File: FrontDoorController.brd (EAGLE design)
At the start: 31.4 x 49.1 mm, 9 parts

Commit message: Door_Control_PCB: Add more header pins
Add more header pins to be able to measure all voltages, and connect to
the limit switches on the Lockitron to log the deadbolt position.  Also
reroute the motor drive wires to not go through the Photon through hole
pins and make the wires larger to drive more current.
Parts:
- JP1: device SparkFun-Connectors:1X05 -> SparkFun-Connectors:1X10_LOCK
- moved JP1 6.69 mm to (3.97, 3.34)
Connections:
- removed net D0: U$1.13, U$3.13
- removed net D1: U$1.14, U$3.14
- new net N$7: JP1.10
- new net SW1: JP1.8, U$1.13, U$3.13
- new net SW2: JP1.9, U$1.14, U$3.14
- net 3V3: now also JP1.6
- net VIN: now also JP1.5
- net VM: now also JP1.7; no longer JP1.5
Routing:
- net 3V3: track 1.27 -> 60.3 mm
- net SW2: track 0.00 -> 18.1 mm
- net SW1: track 0.00 -> 17.3 mm
- net VIN: track 67.9 -> 72.9 mm
- net A02: track 40.2 -> 35.9 mm
- net A01: track 35.9 -> 31.7 mm
- net D1: track 1.27 -> 0.00 mm
- net D0: track 1.27 -> 0.00 mm
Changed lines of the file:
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@@
 <attribute name="NAME" x="16.291" y="40.1415" size="0.4064" layer="26" rot="MR180"/>
 </element>
-<element name="JP1" library="SparkFun-Connectors" package="1X05" value="" x="10.66" y="3.32" smashed="yes">
-<attribute name="VALUE" x="9.39" y="0.145" size="1.27" layer="27"/>
+<element name="JP1" library="SparkFun-Connectors" package="1X10_LOCK" value="" x="3.97" y="3.34" smashed="yes">
+<attribute name="VALUE" x="2.7" y="0.165" size="1.27" layer="27"/>
 </element>
 <element name="D1" library="SparkFun-DiscreteSemi" package="DIODE-1N4001" value="" x="15.67" y="7.01" smashed="yes" rot="R180">
@@
 <wire x1="10.59" y1="7.01" x2="5.99" y2="7.01" width="1.016" layer="1"/>
 <wire x1="5.99" y1="7.01" x2="2" y2="11" width="1.016" layer="1"/>
+<contactref element="JP1" pad="5"/>
+<wire x1="10.59" y1="7.01" x2="10.59" y2="7.007" width="1.016" layer="1"/>
+<wire x1="10.59" y1="7.007" x2="14.13" y2="3.467" width="1.016" layer="1"/>
 </signal>
 <signal name="GND">
@@
 <contactref element="JP1" pad="4"/>
 <contactref element="JP1" pad="3"/>
-<polygon width="0.4064" layer="16">
+<polygon width="0.4064" layer="16" thermals="no">
 <vertex x="1" y="48"/>
 <vertex x="28" y="48"/>
@@
 <wire x1="25.89" y1="44.418" x2="24.63" y2="44.418" width="1.016" layer="1"/>
 <wire x1="24.63" y1="44.418" x2="24.62" y2="44.428" width="1.016" layer="1"/>
+<contactref element="JP1" pad="6"/>
+<wire x1="16.67" y1="3.213" x2="16.67" y2="2.11" width="0.4064" layer="16"/>
+<wire x1="29.02" y1="2.96" x2="29.02" y2="42.88" width="0.4064" layer="16"/>
+<wire x1="29.02" y1="42.88" x2="27.55" y2="44.35" width="0.4064" layer="16"/>
+<wire x1="27.55" y1="44.35" x2="24.698" y2="44.35" width="0.4064" layer="16"/>
+<wire x1="24.698" y1="44.35" x2="24.62" y2="44.428" width="0.4064" layer="16"/>
+<wire x1="16.67" y1="2.11" x2="17.04" y2="1.74" width="0.4064" layer="16"/>
+<wire x1="17.04" y1="1.74" x2="27.8" y2="1.74" width="0.4064" layer="16"/>
+<wire x1="27.8" y1="1.74" x2="29.02" y2="2.96" width="0.4064" layer="16"/>
 </signal>
 <signal name="RSTB">
@@
 <wire x1="25.88" y1="21.568" x2="25.89" y2="21.558" width="1.016" layer="1"/>
 </signal>
-<signal name="D1">
-<contactref element="U$1" pad="14"/>
-<contactref element="U$3" pad="14"/>
-<wire x1="24.62" y1="19.028" x2="25.88" y2="19.028" width="1.016" layer="1"/>
-<wire x1="25.88" y1="19.028" x2="25.89" y2="19.018" width="1.016" layer="1"/>
-</signal>
-<signal name="D0">
-<contactref element="U$1" pad="13"/>
-<contactref element="U$3" pad="13"/>
-<wire x1="24.62" y1="16.488" x2="25.88" y2="16.488" width="1.016" layer="1"/>
-<wire x1="25.88" y1="16.488" x2="25.89" y2="16.478" width="1.016" layer="1"/>
-</signal>
 <signal name="USB_D+">
 <contactref element="U$1" pad="31"/>
@@
 <contactref element="U$2" pad="2"/>
 <contactref element="JP1" pad="2"/>
-<wire x1="12.584" y1="30.155" x2="12.584" y2="30.805" width="0.4064" layer="16"/>
-<wire x1="12.584" y1="30.155" x2="12.584" y2="25.144" width="0.4064" layer="16"/>
-<wire x1="12.584" y1="25.144" x2="5.92" y2="18.48" width="0.4064" layer="16"/>
-<wire x1="5.92" y1="7.22" x2="5.92" y2="18.48" width="0.4064" layer="16"/>
-<wire x1="5.92" y1="7.22" x2="8" y2="5.14" width="0.4064" layer="16"/>
-<wire x1="8" y1="5.14" x2="12.47" y2="5.14" width="0.4064" layer="16"/>
-<wire x1="12.47" y1="5.14" x2="13.2" y2="4.41" width="0.4064" layer="16"/>
-<wire x1="13.2" y1="4.41" x2="13.2" y2="3.32" width="0.4064" layer="16"/>
+<wire x1="12.584" y1="30.805" x2="11.885" y2="30.805" width="0.4064" layer="16"/>
+<wire x1="11.885" y1="30.805" x2="11.52" y2="30.44" width="0.4064" layer="16"/>
+<wire x1="11.52" y1="30.44" x2="11.805" y2="30.155" width="0.4064" layer="16"/>
+<wire x1="11.805" y1="30.155" x2="12.584" y2="30.155" width="0.4064" layer="16"/>
+<wire x1="6.51" y1="3.213" x2="6.51" y2="10.51" width="1.016" layer="16"/>
+<wire x1="6.51" y1="10.51" x2="11" y2="15" width="1.016" layer="16"/>
+<wire x1="11" y1="15" x2="11" y2="29.92" width="1.016" layer="16"/>
+<wire x1="11" y1="29.92" x2="11.52" y2="30.44" width="1.016" layer="16"/>
 </signal>
 <signal name="A02">
@@
 <contactref element="U$2" pad="6"/>
 <contactref element="JP1" pad="1"/>
-<wire x1="12.584" y1="33.405" x2="12.584" y2="32.755" width="0.4064" layer="16"/>
-<wire x1="12.584" y1="32.755" x2="11.095" y2="32.755" width="0.4064" layer="16"/>
-<wire x1="11.095" y1="32.755" x2="10.45" y2="32.11" width="0.4064" layer="16"/>
-<wire x1="10.45" y1="32.11" x2="10.45" y2="25.58" width="0.4064" layer="16"/>
-<wire x1="10.45" y1="25.58" x2="3.94" y2="19.07" width="0.4064" layer="16"/>
-<wire x1="3.94" y1="19.07" x2="3.94" y2="5.06" width="0.4064" layer="16"/>
-<wire x1="3.94" y1="5.06" x2="5.68" y2="3.32" width="0.4064" layer="16"/>
-<wire x1="5.68" y1="3.32" x2="10.66" y2="3.32" width="0.4064" layer="16"/>
+<wire x1="12.584" y1="32.755" x2="11.915" y2="32.755" width="0.4064" layer="16"/>
+<wire x1="11.915" y1="32.755" x2="11.59" y2="33.08" width="0.4064" layer="16"/>
+<wire x1="11.59" y1="33.08" x2="11.915" y2="33.405" width="0.4064" layer="16"/>
+<wire x1="11.915" y1="33.405" x2="12.584" y2="33.405" width="0.4064" layer="16"/>
+<wire x1="3.97" y1="3.467" x2="3.97" y2="9.97" width="1.016" layer="16"/>
+<wire x1="3.97" y1="9.97" x2="9" y2="15" width="1.016" layer="16"/>
+<wire x1="9" y1="15" x2="9" y2="32" width="1.016" layer="16"/>
+<wire x1="9" y1="32" x2="10.08" y2="33.08" width="1.016" layer="16"/>
+<wire x1="10.08" y1="33.08" x2="11.59" y2="33.08" width="1.016" layer="16"/>
 </signal>
 <signal name="VM">
@@
 <contactref element="U$2" pad="24"/>
 <contactref element="C1" pad="A"/>
-<contactref element="JP1" pad="5"/>
 <contactref element="C2" pad="1"/>
 <wire x1="18.14" y1="24.76" x2="18.07" y2="24.76" width="0.4064" layer="16"/>
@@
 <wire x1="18.1" y1="36.685" x2="18.1" y2="36.76" width="0.4064" layer="16"/>
 <contactref element="D1" pad="A"/>
-<polygon width="0.4064" layer="1">
+<polygon width="0.4064" layer="1" thermals="no">
 <vertex x="1" y="48"/>
 <vertex x="28" y="48"/>
@@
 <wire x1="18.345" y1="36.655" x2="18.205" y2="36.655" width="0.6096" layer="16"/>
 <wire x1="18.205" y1="36.655" x2="18.1" y2="36.76" width="0.6096" layer="16" curve="-90"/>
+<contactref element="JP1" pad="7"/>
 </signal>
 <signal name="N$3">
@@
 <wire x1="24.63" y1="39.338" x2="24.62" y2="39.348" width="1.016" layer="1"/>
 </signal>
+<signal name="SW1">
+<contactref element="JP1" pad="8"/>
+<contactref element="U$1" pad="13"/>
+<wire x1="21.75" y1="3.213" x2="21.75" y2="4.75" width="0.4064" layer="16"/>
+<wire x1="21.75" y1="4.75" x2="25" y2="8" width="0.4064" layer="16"/>
+<contactref element="U$3" pad="13"/>
+<wire x1="24.62" y1="16.488" x2="25.88" y2="16.488" width="1.016" layer="1"/>
+<wire x1="25.89" y1="16.478" x2="24.63" y2="16.478" width="0.4064" layer="1"/>
+<wire x1="24.63" y1="16.478" x2="24.62" y2="16.488" width="0.4064" layer="1"/>
+<wire x1="25" y1="8" x2="25" y2="16.108" width="0.4064" layer="16"/>
+<wire x1="25" y1="16.108" x2="24.62" y2="16.488" width="0.4064" layer="16"/>
+</signal>
+<signal name="SW2">
+<contactref element="JP1" pad="9"/>
+<contactref element="U$1" pad="14"/>
+<contactref element="U$3" pad="14"/>
+<wire x1="24.62" y1="19.028" x2="25.88" y2="19.028" width="1.016" layer="1"/>
+<wire x1="24.29" y1="3.467" x2="24.29" y2="6.29" width="0.4064" layer="16"/>
+<wire x1="24.29" y1="6.29" x2="26" y2="8" width="0.4064" layer="16"/>
+<wire x1="26" y1="8" x2="26" y2="17.648" width="0.4064" layer="16"/>
+<wire x1="26" y1="17.648" x2="24.62" y2="19.028" width="0.4064" layer="16"/>
+<wire x1="25.88" y1="19.028" x2="25.89" y2="19.018" width="0" layer="19" extent="1-1"/>
+</signal>
+<signal name="N$7">
+<contactref element="JP1" pad="10"/>
+</signal>
 </signals>

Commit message: Door_Control_PCB: Add reed switch connection
Add a connection point for a reed switch to be used to sense if the door
is open or closed.  Also add a pull down resistor to ensure good
readings and label the pins on the header.
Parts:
- added R1: 1K, SparkFun-Resistors:0603-RES
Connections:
- removed net D2: U$1.15, U$3.15
- removed net N$7: JP1.10
- new net DOORSW: JP1.10, R1.2, U$1.15, U$3.15
- net GND: now also R1.1
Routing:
- net DOORSW: track 0.00 -> 25.0 mm
- net D2: track 1.27 -> 0.00 mm
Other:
- board text added: "3V3"
- board text added: "A01"
- board text added: "A02"
- board text added: "DOORSW"
- board text added: "GND"
- board text added: "SW1"
- board text added: "SW2"
- board text added: "VIN"
- board text added: "VM"
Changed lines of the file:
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@@
 <dimension x1="0" y1="0" x2="0" y2="49" x3="-4" y3="24.5" textsize="1.778" layer="48" unit="inch"/>
 <dimension x1="0" y1="0" x2="31.42" y2="0" x3="15.71" y3="-4" textsize="1.778" layer="48" unit="inch"/>
+<text x="3.13" y="1" size="0.6096" layer="51">A02</text>
+<text x="5.7" y="1" size="0.6096" layer="51">A01</text>
+<text x="9.45" y="1" size="0.6096" layer="51">GND</text>
+<text x="13.35" y="1" size="0.6096" layer="51">VIN</text>
+<text x="16" y="1" size="0.6096" layer="51">3V3</text>
+<text x="18.59" y="1.01" size="0.6096" layer="51">VM</text>
+<text x="20.82" y="1" size="0.6096" layer="51">SW1</text>
+<text x="23.4" y="1" size="0.6096" layer="51">SW2</text>
+<text x="26" y="1" size="0.6096" layer="51">DOORSW</text>
 </plain>
 <attributes>
@@
 </element>
 <element name="U$3" library="Spark" package="PHOTON" value="PHOTON_WITH_HEADERS" x="5.57" y="12.17" smashed="yes"/>
+<element name="R1" library="SparkFun-Resistors" package="0603-RES" value="1K" x="21.5" y="21.69" rot="MR180"/>
 </elements>
 <signals>
@@
 <wire x1="25.89" y1="36.79" x2="24.638" y2="36.79" width="1.016" layer="1"/>
 <wire x1="24.638" y1="36.79" x2="24.62" y2="36.808" width="1.016" layer="1"/>
+<contactref element="R1" pad="1"/>
 </signal>
 <signal name="TX">
@@
 <wire x1="19.896" y1="33.405" x2="22.943" y2="33.405" width="0.4064" layer="16"/>
 <wire x1="22.943" y1="33.405" x2="24.62" y2="31.728" width="0.4064" layer="16"/>
-</signal>
-<signal name="D2">
-<contactref element="U$1" pad="15"/>
-<contactref element="U$3" pad="15"/>
-<wire x1="24.62" y1="21.568" x2="25.88" y2="21.568" width="1.016" layer="1"/>
-<wire x1="25.88" y1="21.568" x2="25.89" y2="21.558" width="1.016" layer="1"/>
 </signal>
 <signal name="USB_D+">
@@
 <wire x1="25.88" y1="19.028" x2="25.89" y2="19.018" width="0" layer="19" extent="1-1"/>
 </signal>
-<signal name="N$7">
+<signal name="DOORSW">
 <contactref element="JP1" pad="10"/>
+<contactref element="U$1" pad="15"/>
+<contactref element="U$3" pad="15"/>
+<wire x1="24.62" y1="21.568" x2="25.88" y2="21.568" width="1.016" layer="1"/>
+<wire x1="26.83" y1="3.213" x2="29" y2="5.383" width="0.4064" layer="1"/>
+<wire x1="27.442" y1="21.558" x2="25.89" y2="21.558" width="0.4064" layer="1"/>
+<wire x1="29" y1="5.383" x2="29" y2="20" width="0.4064" layer="1"/>
+<wire x1="29" y1="20" x2="27.442" y2="21.558" width="0.4064" layer="1"/>
+<contactref element="R1" pad="2"/>
+<wire x1="24.62" y1="21.568" x2="24.498" y2="21.69" width="0.4064" layer="16"/>
+<wire x1="24.498" y1="21.69" x2="22.35" y2="21.69" width="0.4064" layer="16"/>
+<wire x1="25.89" y1="21.558" x2="25.88" y2="21.568" width="0" layer="19" extent="1-1"/>
 </signal>
 </signals>

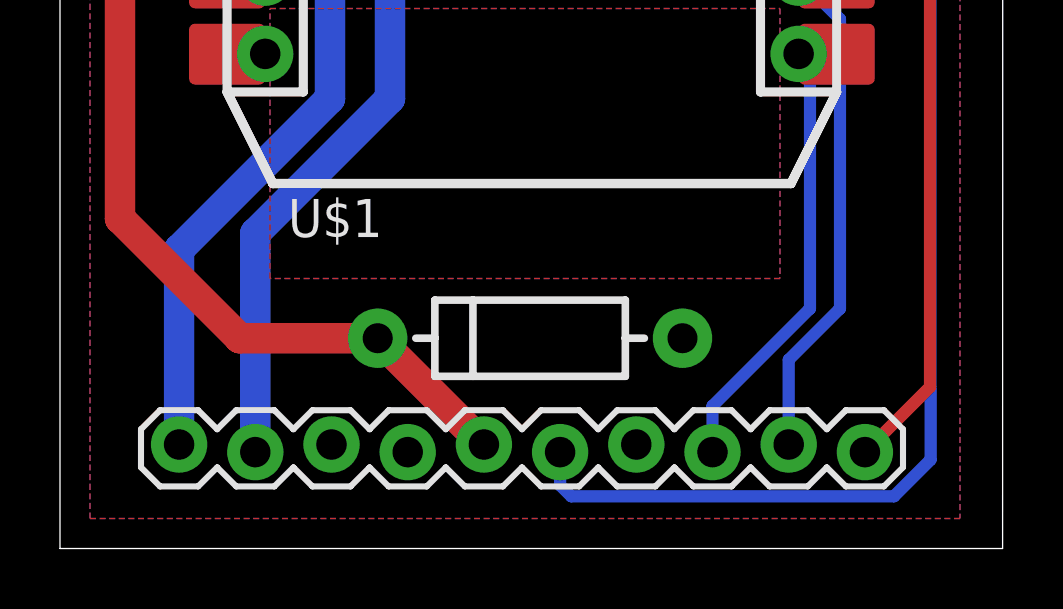
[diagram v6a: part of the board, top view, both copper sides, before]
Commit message: Door_Control_PCB: Change layer of labels
Change the layer of the header labels because they didn't show up on Osh
Park.
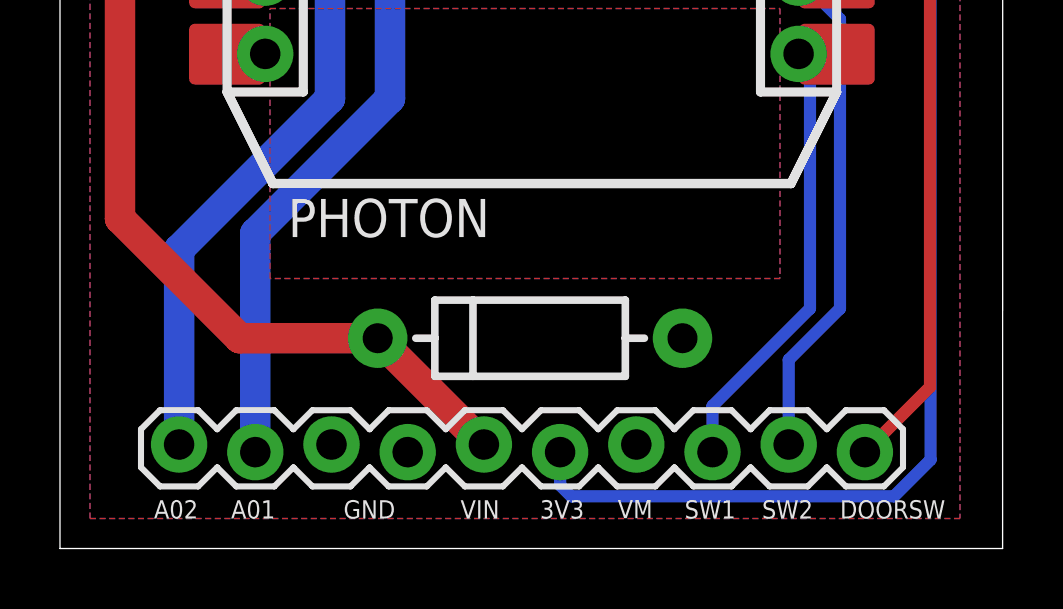
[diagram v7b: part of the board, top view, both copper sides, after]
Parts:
- renumbered U$1 to PHOTON
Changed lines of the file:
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@@
 <dimension x1="0" y1="0" x2="0" y2="49" x3="-4" y3="24.5" textsize="1.778" layer="48" unit="inch"/>
 <dimension x1="0" y1="0" x2="31.42" y2="0" x3="15.71" y3="-4" textsize="1.778" layer="48" unit="inch"/>
-<text x="3.13" y="1" size="0.6096" layer="51">A02</text>
-<text x="5.7" y="1" size="0.6096" layer="51">A01</text>
-<text x="9.45" y="1" size="0.6096" layer="51">GND</text>
-<text x="13.35" y="1" size="0.6096" layer="51">VIN</text>
-<text x="16" y="1" size="0.6096" layer="51">3V3</text>
-<text x="18.59" y="1.01" size="0.6096" layer="51">VM</text>
-<text x="20.82" y="1" size="0.6096" layer="51">SW1</text>
-<text x="23.4" y="1" size="0.6096" layer="51">SW2</text>
-<text x="26" y="1" size="0.6096" layer="51">DOORSW</text>
+<text x="3.13" y="1" size="0.6096" layer="25">A02</text>
+<text x="5.7" y="1" size="0.6096" layer="25">A01</text>
+<text x="9.45" y="1" size="0.6096" layer="25">GND</text>
+<text x="13.35" y="1" size="0.6096" layer="25">VIN</text>
+<text x="16" y="1" size="0.6096" layer="25">3V3</text>
+<text x="18.59" y="1.01" size="0.6096" layer="25">VM</text>
+<text x="20.82" y="1" size="0.6096" layer="25">SW1</text>
+<text x="23.4" y="1" size="0.6096" layer="25">SW2</text>
+<text x="26" y="1" size="0.6096" layer="25">DOORSW</text>
 </plain>
 <attributes>
@@
 </autorouter>
 <elements>
-<element name="U$1" library="Spark" package="PHOTON_SMD" value="PHOTON_SMD" x="5.57" y="12.16"/>
+<element name="PHOTON" library="Spark" package="PHOTON_SMD" value="PHOTON_SMD" x="5.57" y="12.16" smashed="yes">
+<attribute name="NAME" x="7.602" y="10.382" size="1.27" layer="25" ratio="10"/>
+<attribute name="VALUE" x="7.602" y="8.858" size="1.27" layer="27"/>
+</element>
 <element name="FRAME1" library="SparkFun-Aesthetics" package="CREATIVE_COMMONS" value="FRAME-LETTER" x="87" y="34"/>
 <element name="U$2" library="SparkFun-PowerIC" package="SSOP24" value="TB6612FNG" x="16.24" y="33.73" rot="MR90">
@@
 <signals>
 <signal name="VIN">
-<contactref element="U$1" pad="1"/>
+<contactref element="PHOTON" pad="1"/>
 <contactref element="D1" pad="C"/>
 <wire x1="2" y1="11" x2="2" y2="43" width="1.016" layer="1"/>
@@
 </signal>
 <signal name="GND">
-<contactref element="U$1" pad="2"/>
-<contactref element="U$1" pad="21"/>
+<contactref element="PHOTON" pad="2"/>
+<contactref element="PHOTON" pad="21"/>
 <contactref element="U$2" pad="18"/>
 <contactref element="C3" pad="2"/>
@@
 </signal>
 <signal name="TX">
-<contactref element="U$1" pad="3"/>
+<contactref element="PHOTON" pad="3"/>
 <contactref element="U$3" pad="3"/>
 <wire x1="5.57" y1="39.338" x2="6.83" y2="39.338" width="1.016" layer="1"/>
@@
 </signal>
 <signal name="RX">
-<contactref element="U$1" pad="4"/>
+<contactref element="PHOTON" pad="4"/>
 <contactref element="U$3" pad="4"/>
 <wire x1="5.57" y1="36.798" x2="6.83" y2="36.798" width="1.016" layer="1"/>
@@
 </signal>
 <signal name="WKP">
-<contactref element="U$1" pad="5"/>
+<contactref element="PHOTON" pad="5"/>
 <contactref element="U$3" pad="5"/>
 <wire x1="5.57" y1="34.258" x2="6.83" y2="34.258" width="1.016" layer="1"/>
@@
 </signal>
 <signal name="DAC">
-<contactref element="U$1" pad="6"/>
+<contactref element="PHOTON" pad="6"/>
 <contactref element="U$3" pad="6"/>
 <wire x1="5.57" y1="31.718" x2="6.83" y2="31.718" width="1.016" layer="1"/>
@@
 </signal>
 <signal name="A5">
-<contactref element="U$1" pad="7"/>
+<contactref element="PHOTON" pad="7"/>
 <contactref element="U$3" pad="7"/>
 <wire x1="5.57" y1="29.178" x2="6.83" y2="29.178" width="1.016" layer="1"/>
@@
 </signal>
 <signal name="A4">
-<contactref element="U$1" pad="8"/>
+<contactref element="PHOTON" pad="8"/>
 <contactref element="U$3" pad="8"/>
 <wire x1="5.57" y1="26.638" x2="6.83" y2="26.638" width="1.016" layer="1"/>
@@
 </signal>
 <signal name="A3">
-<contactref element="U$1" pad="9"/>
+<contactref element="PHOTON" pad="9"/>
 <contactref element="U$3" pad="9"/>
 <wire x1="5.57" y1="24.098" x2="6.83" y2="24.098" width="1.016" layer="1"/>
@@
 </signal>
 <signal name="A2">
-<contactref element="U$1" pad="10"/>
+<contactref element="PHOTON" pad="10"/>
 <contactref element="U$3" pad="10"/>
 <wire x1="5.57" y1="21.558" x2="6.83" y2="21.558" width="1.016" layer="1"/>
@@
 </signal>
 <signal name="A1">
-<contactref element="U$1" pad="11"/>
+<contactref element="PHOTON" pad="11"/>
 <contactref element="U$3" pad="11"/>
 <wire x1="5.57" y1="19.018" x2="6.83" y2="19.018" width="1.016" layer="1"/>
@@
 </signal>
 <signal name="A0">
-<contactref element="U$1" pad="12"/>
+<contactref element="PHOTON" pad="12"/>
 <contactref element="U$3" pad="12"/>
 <wire x1="5.57" y1="16.478" x2="6.83" y2="16.478" width="1.016" layer="1"/>
@@
 </signal>
 <signal name="3V3">
-<contactref element="U$1" pad="24"/>
+<contactref element="PHOTON" pad="24"/>
 <contactref element="U$3" pad="24"/>
 <wire x1="25.89" y1="44.418" x2="24.63" y2="44.418" width="1.016" layer="1"/>
@@
 </signal>
 <signal name="RSTB">
-<contactref element="U$1" pad="23"/>
+<contactref element="PHOTON" pad="23"/>
 <contactref element="U$3" pad="23"/>
 <wire x1="25.89" y1="41.878" x2="24.63" y2="41.878" width="1.016" layer="1"/>
@@
 </signal>
 <signal name="D7">
-<contactref element="U$1" pad="20"/>
+<contactref element="PHOTON" pad="20"/>
 <contactref element="U$3" pad="20"/>
 <wire x1="25.89" y1="34.258" x2="24.63" y2="34.258" width="1.016" layer="1"/>
@@
 </signal>
 <signal name="PWMA">
-<contactref element="U$1" pad="16"/>
+<contactref element="PHOTON" pad="16"/>
 <contactref element="U$2" pad="23"/>
 <contactref element="U$3" pad="16"/>
@@
 </signal>
 <signal name="STBY">
-<contactref element="U$1" pad="19"/>
+<contactref element="PHOTON" pad="19"/>
 <contactref element="U$2" pad="19"/>
 <contactref element="U$3" pad="19"/>
@@
 </signal>
 <signal name="USB_D+">
-<contactref element="U$1" pad="31"/>
+<contactref element="PHOTON" pad="31"/>
 </signal>
 <signal name="USB_D-">
-<contactref element="U$1" pad="30"/>
+<contactref element="PHOTON" pad="30"/>
 </signal>
 <signal name="RGB_BLUE">
-<contactref element="U$1" pad="29"/>
+<contactref element="PHOTON" pad="29"/>
 </signal>
 <signal name="RGB_GREEN">
-<contactref element="U$1" pad="28"/>
+<contactref element="PHOTON" pad="28"/>
 </signal>
 <signal name="RGB_RED">
-<contactref element="U$1" pad="27"/>
+<contactref element="PHOTON" pad="27"/>
 </signal>
 <signal name="SETUPB">
-<contactref element="U$1" pad="26"/>
+<contactref element="PHOTON" pad="26"/>
 </signal>
 <signal name="EN">
-<contactref element="U$1" pad="25"/>
+<contactref element="PHOTON" pad="25"/>
 </signal>
 <signal name="A01">
@@
 <signal name="AIN1">
 <contactref element="U$2" pad="21"/>
-<contactref element="U$1" pad="18"/>
+<contactref element="PHOTON" pad="18"/>
 <contactref element="U$3" pad="18"/>
 <wire x1="25.89" y1="29.178" x2="24.63" y2="29.178" width="1.016" layer="1"/>
@@
 <signal name="AIN2">
 <contactref element="U$2" pad="22"/>
-<contactref element="U$1" pad="17"/>
+<contactref element="PHOTON" pad="17"/>
 <contactref element="U$3" pad="17"/>
 <wire x1="24.62" y1="26.648" x2="25.88" y2="26.648" width="1.016" layer="1"/>
@@
 </signal>
 <signal name="VBAT">
-<contactref element="U$1" pad="22"/>
+<contactref element="PHOTON" pad="22"/>
 <contactref element="U$3" pad="22"/>
 <wire x1="25.89" y1="39.338" x2="24.63" y2="39.338" width="1.016" layer="1"/>
@@
 <signal name="SW1">
 <contactref element="JP1" pad="8"/>
-<contactref element="U$1" pad="13"/>
+<contactref element="PHOTON" pad="13"/>
 <wire x1="21.75" y1="3.213" x2="21.75" y2="4.75" width="0.4064" layer="16"/>
 <wire x1="21.75" y1="4.75" x2="25" y2="8" width="0.4064" layer="16"/>
@@
 <signal name="SW2">
 <contactref element="JP1" pad="9"/>
-<contactref element="U$1" pad="14"/>
+<contactref element="PHOTON" pad="14"/>
 <contactref element="U$3" pad="14"/>
 <wire x1="24.62" y1="19.028" x2="25.88" y2="19.028" width="1.016" layer="1"/>
@@
 <signal name="DOORSW">
 <contactref element="JP1" pad="10"/>
-<contactref element="U$1" pad="15"/>
+<contactref element="PHOTON" pad="15"/>
 <contactref element="U$3" pad="15"/>
 <wire x1="24.62" y1="21.568" x2="25.88" y2="21.568" width="1.016" layer="1"/>
